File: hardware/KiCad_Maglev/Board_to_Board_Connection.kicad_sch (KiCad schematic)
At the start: 4 parts, among them J11 690367190672, J12 690367190672, J7 690367191672, J8 690367191672

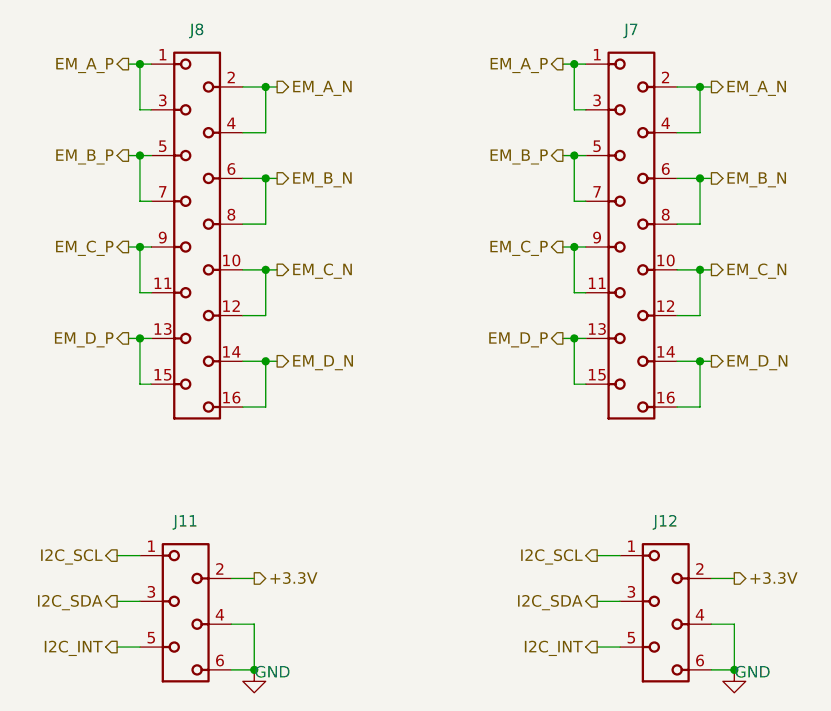
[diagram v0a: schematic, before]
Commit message: changed usb-c connector because pcbway cant handle the old one, cleared all design rule errors
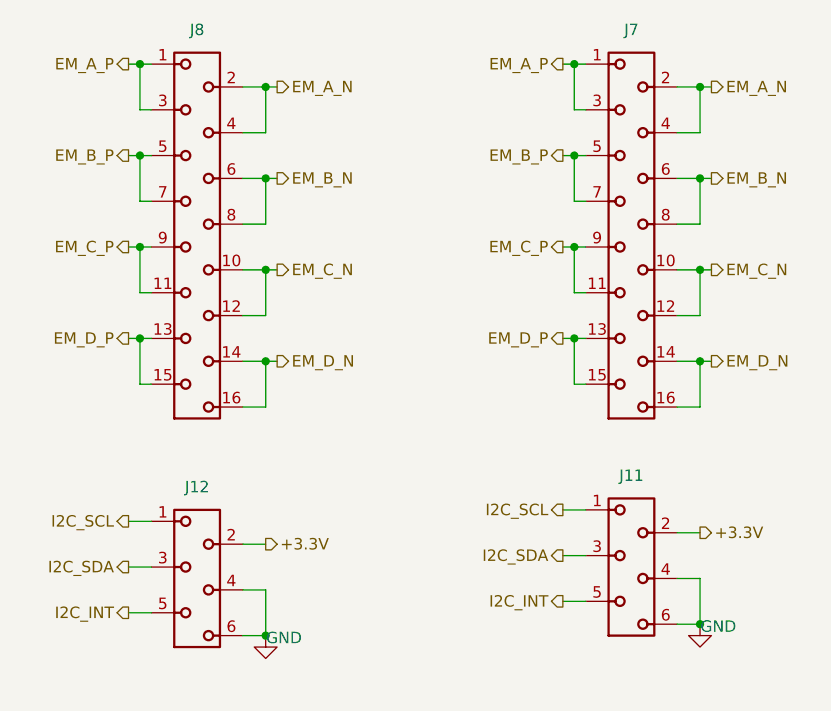
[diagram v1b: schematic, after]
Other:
- moved on the sheet: J11, J12
